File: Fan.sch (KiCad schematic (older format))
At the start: 0 parts

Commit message: Created CurrentDriver, Relay, and PowerProtection modules
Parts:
- added Q?: MOSFET_N, ~, symbol MOSFET_N
- added R? (x4): R, ~, symbol R
- added RV?: POT, ~, symbol POT
- added U?: LM324, symbol LM324
- added U?: MCP4922-E/P, DIP14, symbol MCP4922-E/P
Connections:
- net labels added: +12V, -12V, AGND, CS_N, Current Measure, MISO, MOSI, SCLK
- wire segments 0 -> 29

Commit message: Current driver refactoring, LED module, Arduino
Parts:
- removed R? (x2): R, ~, symbol R
- removed RV?: POT, ~, symbol POT
- added D?: DIODE, ~, symbol DIODE
- added Q? (x2): MOSFET_N, ~, symbol MOSFET_N
- added TH?: THERMISTOR, ~, symbol THERMISTOR
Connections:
- net labels added: +12C, CURR_MEAS, FAN_MODE, FAN_OUT+, FAN_OUT-, FAN_PWM, TACH_IN, TACH_MEAS
- net labels removed: Current Measure, Fan_In, Power+, Power-, Tach, Tach_out
- wire segments 29 -> 34
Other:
- moved on the sheet: R?, U?
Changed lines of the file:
@@
 Comment4 ""
 $EndDescr
-Text HLabel 10150 3200 0    60   Output ~ 0
-Power+
-Text HLabel 10150 3550 0    60   Input ~ 0
-Power-
-Text HLabel 10150 3950 0    60   Input ~ 0
-Tach
-Text HLabel 1400 4950 0    60   Output ~ 0
-Tach_out
-Text HLabel 1400 3650 0    60   Input ~ 0
-Fan_In
+Text HLabel 9950 1700 2    60   Output ~ 0
+FAN_OUT+
+Text HLabel 9950 2000 2    60   Output ~ 0
+FAN_OUT-
+Text HLabel 10400 6150 2    60   Input ~ 0
+TACH_IN
+Text HLabel 1400 6150 0    60   Output ~ 0
+TACH_MEAS
+Text HLabel 1300 3650 0    60   Input ~ 0
+FAN_PWM
 $Comp
 L LM324 U?
@@
 $EndComp
 $Comp
-L +12V #PWR?
-U 1 1 52F44494
-P 6600 1950
-F 0 "#PWR?" H 6600 1900 20  0001 C CNN
-F 1 "+12V" H 6600 2050 30  0000 C CNN
-F 2 "" H 6600 1950 60  0000 C CNN
-F 3 "" H 6600 1950 60  0000 C CNN
-	1    6600 1950
-	1    0    0    -1
-$EndComp
-$Comp
 L R R?
 U 1 1 52F444AC
@@
 L AGND #PWR?
 U 1 1 52F444C1
-P 6600 4750
-F 0 "#PWR?" H 6600 4750 40  0001 C CNN
-F 1 "AGND" H 6600 4680 50  0000 C CNN
-F 2 "" H 6600 4750 60  0000 C CNN
-F 3 "" H 6600 4750 60  0000 C CNN
-	1    6600 4750
+P 6600 4900
+F 0 "#PWR?" H 6600 4900 40  0001 C CNN
+F 1 "AGND" H 6600 4830 50  0000 C CNN
+F 2 "" H 6600 4900 60  0000 C CNN
+F 3 "" H 6600 4900 60  0000 C CNN
+	1    6600 4900
 	1    0    0    -1
 $EndComp
@@
 $EndComp
 $Comp
+L AGND #PWR?
+U 1 1 52F44588
+P 3700 3500
+F 0 "#PWR?" H 3700 3500 40  0001 C CNN
+F 1 "AGND" H 3700 3430 50  0000 C CNN
+F 2 "" H 3700 3500 60  0000 C CNN
+F 3 "" H 3700 3500 60  0000 C CNN
+	1    3700 3500
+	1    0    0    -1
+$EndComp
+$Comp
+L MCP4922-E/P U?
+U 1 1 52F445A1
+P 2100 2550
+F 0 "U?" H 2250 2950 40  0000 L BNN
+F 1 "MCP4922-E/P" H 2250 2900 40  0000 L BNN
+F 2 "DIP14" H 2100 2550 30  0000 C CIN
+F 3 "" H 2100 2550 60  0000 C CNN
+	1    2100 2550
+	1    0    0    -1
+$EndComp
+Text HLabel 1300 3850 0    60   Output ~ 0
+CURR_MEAS
+Text HLabel 1000 2350 0    60   Input ~ 0
+MOSI
+Text HLabel 1000 2650 0    60   Output ~ 0
+MISO
+Text HLabel 1000 2550 0    60   Input ~ 0
+CS_N
+Text HLabel 1000 2450 0    60   Input ~ 0
+SCLK
+Wire Wire Line
+	5450 2500 6300 2500
+Wire Wire Line
+	6600 2700 6600 4100
+Wire Wire Line
+	6600 4600 6600 4900
+Wire Wire Line
+	4100 3550 4100 2600
+Wire Wire Line
+	4100 2600 4450 2600
+Connection ~ 6600 3550
+Wire Wire Line
+	4850 1950 4850 2100
+Wire Wire Line
+	4850 3000 4850 2900
+Wire Wire Line
+	1300 3850 6600 3850
+Connection ~ 6600 3850
+Wire Wire Line
+	1000 2350 1550 2350
+Wire Wire Line
+	1000 2450 1550 2450
+Wire Wire Line
+	1000 2550 1550 2550
+$Comp
 L R R?
 U 1 1 52F44520
-P 3300 2050
-F 0 "R?" V 3380 2050 40  0000 C CNN
-F 1 "R" V 3307 2051 40  0000 C CNN
-F 2 "~" V 3230 2050 30  0000 C CNN
-F 3 "~" H 3300 2050 30  0000 C CNN
-	1    3300 2050
-	1    0    0    -1
-$EndComp
-$Comp
-L +12V #PWR?
-U 1 1 52F44526
-P 3300 1700
-F 0 "#PWR?" H 3300 1650 20  0001 C CNN
-F 1 "+12V" H 3300 1800 30  0000 C CNN
-F 2 "" H 3300 1700 60  0000 C CNN
-F 3 "" H 3300 1700 60  0000 C CNN
-	1    3300 1700
-	1    0    0    -1
-$EndComp
-$Comp
-L POT RV?
-U 1 1 52F4455B
-P 3300 2800
-F 0 "RV?" H 3300 2700 50  0000 C CNN
-F 1 "POT" H 3300 2800 50  0000 C CNN
-F 2 "~" H 3300 2800 60  0000 C CNN
-F 3 "~" H 3300 2800 60  0000 C CNN
-	1    3300 2800
+P 3250 2400
+F 0 "R?" V 3330 2400 40  0000 C CNN
+F 1 "R" V 3257 2401 40  0000 C CNN
+F 2 "~" V 3180 2400 30  0000 C CNN
+F 3 "~" H 3250 2400 30  0000 C CNN
+	1    3250 2400
 	0    -1   -1   0
 $EndComp
-$Comp
-L AGND #PWR?
-U 1 1 52F44588
-P 3300 3250
-F 0 "#PWR?" H 3300 3250 40  0001 C CNN
-F 1 "AGND" H 3300 3180 50  0000 C CNN
-F 2 "" H 3300 3250 60  0000 C CNN
-F 3 "" H 3300 3250 60  0000 C CNN
-	1    3300 3250
-	1    0    0    -1
-$EndComp
-$Comp
-L MCP4922-E/P U?
-U 1 1 52F445A1
-P 2200 2500
-F 0 "U?" H 2350 2900 40  0000 L BNN
-F 1 "MCP4922-E/P" H 2350 2850 40  0000 L BNN
-F 2 "DIP14" H 2200 2500 30  0000 C CIN
-F 3 "" H 2200 2500 60  0000 C CNN
-	1    2200 2500
-	1    0    0    -1
-$EndComp
-Text HLabel 1400 3850 0    60   Output ~ 0
-Current Measure
-$Comp
-L R R?
-U 1 1 52F445E4
-P 3800 3050
-F 0 "R?" V 3880 3050 40  0000 C CNN
-F 1 "R" V 3807 3051 40  0000 C CNN
-F 2 "~" V 3730 3050 30  0000 C CNN
-F 3 "~" H 3800 3050 30  0000 C CNN
-	1    3800 3050
-	1    0    0    -1
-$EndComp
-Text HLabel 1100 2300 0    60   Input ~ 0
-MOSI
-Text HLabel 1100 2600 0    60   Output ~ 0
-MISO
-Text HLabel 1100 2500 0    60   Input ~ 0
-CS_N
-Text HLabel 1100 2400 0    60   Input ~ 0
-SCLK
-Wire Wire Line
-	5450 2500 6300 2500
-Wire Wire Line
-	6600 2700 6600 3200
-Wire Wire Line
-	6600 3200 10150 3200
-Wire Wire Line
-	4100 3550 10150 3550
-Wire Wire Line
-	6600 3550 6600 4100
-Wire Wire Line
-	6600 4750 6600 4600
-Wire Wire Line
-	4100 3550 4100 2600
-Wire Wire Line
-	4100 2600 4450 2600
-Connection ~ 6600 3550
-Wire Wire Line
-	6600 2300 6600 1950
-Wire Wire Line
-	4850 1950 4850 2100
-Wire Wire Line
-	4850 3000 4850 2900
-Wire Wire Line
-	3300 2400 4450 2400
-Wire Wire Line
-	3300 1700 3300 1800
-Wire Wire Line
-	3300 3250 3300 3050
-Wire Wire Line
-	1400 4950 9350 4950
-Wire Wire Line
-	9350 4950 9350 3950
-Wire Wire Line
-	9350 3950 10150 3950
-Wire Wire Line
-	1400 3850 5600 3850
-Wire Wire Line
-	5450 3850 6600 3850
-Connection ~ 6600 3850
-Wire Wire Line
-	3300 2300 3300 2550
-Connection ~ 3300 2400
-Wire Wire Line
-	3800 2800 3800 2400
-Connection ~ 3800 2400
-Wire Wire Line
-	1400 3650 3800 3650
-Wire Wire Line
-	3800 3650 3800 3300
-Wire Wire Line
-	1100 2300 1650 2300
-Wire Wire Line
-	1100 2400 1650 2400
-Wire Wire Line
-	1100 2500 1650 2500
-Wire Wire Line
-	1650 2700 1600 2700
-Connection ~ 1600 3650
-$Comp
-L R R?
-U 1 1 52F446FA
-P 1600 3200
-F 0 "R?" V 1680 3200 40  0000 C CNN
-F 1 "R" V 1607 3201 40  0000 C CNN
-F 2 "~" V 1530 3200 30  0000 C CNN
-F 3 "~" H 1600 3200 30  0000 C CNN
-	1    1600 3200
-	1    0    0    -1
-$EndComp
-Wire Wire Line
-	1600 3450 1600 3650
-Wire Wire Line
-	1600 2700 1600 2950
+Wire Wire Line
+	3000 2400 2650 2400
+$Comp
+L MOSFET_N Q?
+U 1 1 52F7C941
+P 5800 4350
+F 0 "Q?" H 5810 4520 60  0000 R CNN
+F 1 "MOSFET_N" H 5810 4200 60  0000 R CNN
+F 2 "~" H 5800 4350 60  0000 C CNN
+F 3 "~" H 5800 4350 60  0000 C CNN
+	1    5800 4350
+	1    0    0    -1
+$EndComp
+$Comp
+L THERMISTOR TH?
+U 1 1 52F7C9A5
+P 6600 1250
+F 0 "TH?" V 6700 1300 50  0000 C CNN
+F 1 "THERMISTOR" V 6500 1250 50  0000 C CNN
+F 2 "~" H 6600 1250 60  0000 C CNN
+F 3 "~" H 6600 1250 60  0000 C CNN
+	1    6600 1250
+	1    0    0    -1
+$EndComp
+Wire Wire Line
+	6600 1500 6600 1700
+Wire Wire Line
+	6600 1700 9950 1700
+Wire Wire Line
+	4100 3550 6600 3550
+Wire Wire Line
+	9950 2000 6600 2000
+Wire Wire Line
+	6600 2000 6600 2300
+Wire Wire Line
+	6600 900  6600 1000
+$Comp
+L DIODE D?
+U 1 1 52F7CA49
+P 6400 1800
+F 0 "D?" H 6400 1900 40  0000 C CNN
+F 1 "DIODE" H 6400 1700 40  0000 C CNN
+F 2 "~" H 6400 1800 60  0000 C CNN
+F 3 "~" H 6400 1800 60  0000 C CNN
+	1    6400 1800
+	0    -1   -1   0
+$EndComp
+Wire Wire Line
+	6400 2000 6400 2100
+Wire Wire Line
+	6400 2100 6600 2100
+Connection ~ 6600 2100
+Wire Wire Line
+	6400 1600 6400 1550
+Wire Wire Line
+	6400 1550 6600 1550
+Connection ~ 6600 1550
+Wire Wire Line
+	5900 4150 5900 4000
+Wire Wire Line
+	5900 4000 6600 4000
+Connection ~ 6600 4000
+Wire Wire Line
+	5900 4550 5900 4700
+Wire Wire Line
+	5900 4700 6600 4700
+Connection ~ 6600 4700
+Wire Wire Line
+	10400 6150 1400 6150
+Wire Wire Line
+	1300 3650 2850 3650
+Wire Wire Line
+	3500 2400 4450 2400
+$Comp
+L MOSFET_N Q?
+U 1 1 52F7CBE7
+P 3600 3100
+F 0 "Q?" H 3610 3270 60  0000 R CNN
+F 1 "MOSFET_N" H 3610 2950 60  0000 R CNN
+F 2 "~" H 3600 3100 60  0000 C CNN
+F 3 "~" H 3600 3100 60  0000 C CNN
+	1    3600 3100
+	1    0    0    -1
+$EndComp
+Wire Wire Line
+	3400 3100 2850 3100
+Wire Wire Line
+	2850 3100 2850 3650
+Wire Wire Line
+	3700 3500 3700 3300
+Wire Wire Line
+	3700 2900 3700 2400
+Connection ~ 3700 2400
+Wire Wire Line
+	5600 4350 1300 4350
+Text HLabel 1300 4350 0    60   Input ~ 0
+FAN_MODE
+$Comp
+L +12C #PWR?
+U 1 1 52F7D01B
+P 6600 900
+F 0 "#PWR?" H 6600 870 30  0001 C CNN
+F 1 "+12C" H 6600 1010 40  0000 C CNN
+F 2 "" H 6600 900 60  0000 C CNN
+F 3 "" H 6600 900 60  0000 C CNN
+	1    6600 900
+	1    0    0    -1
+$EndComp
 $EndSCHEMATC

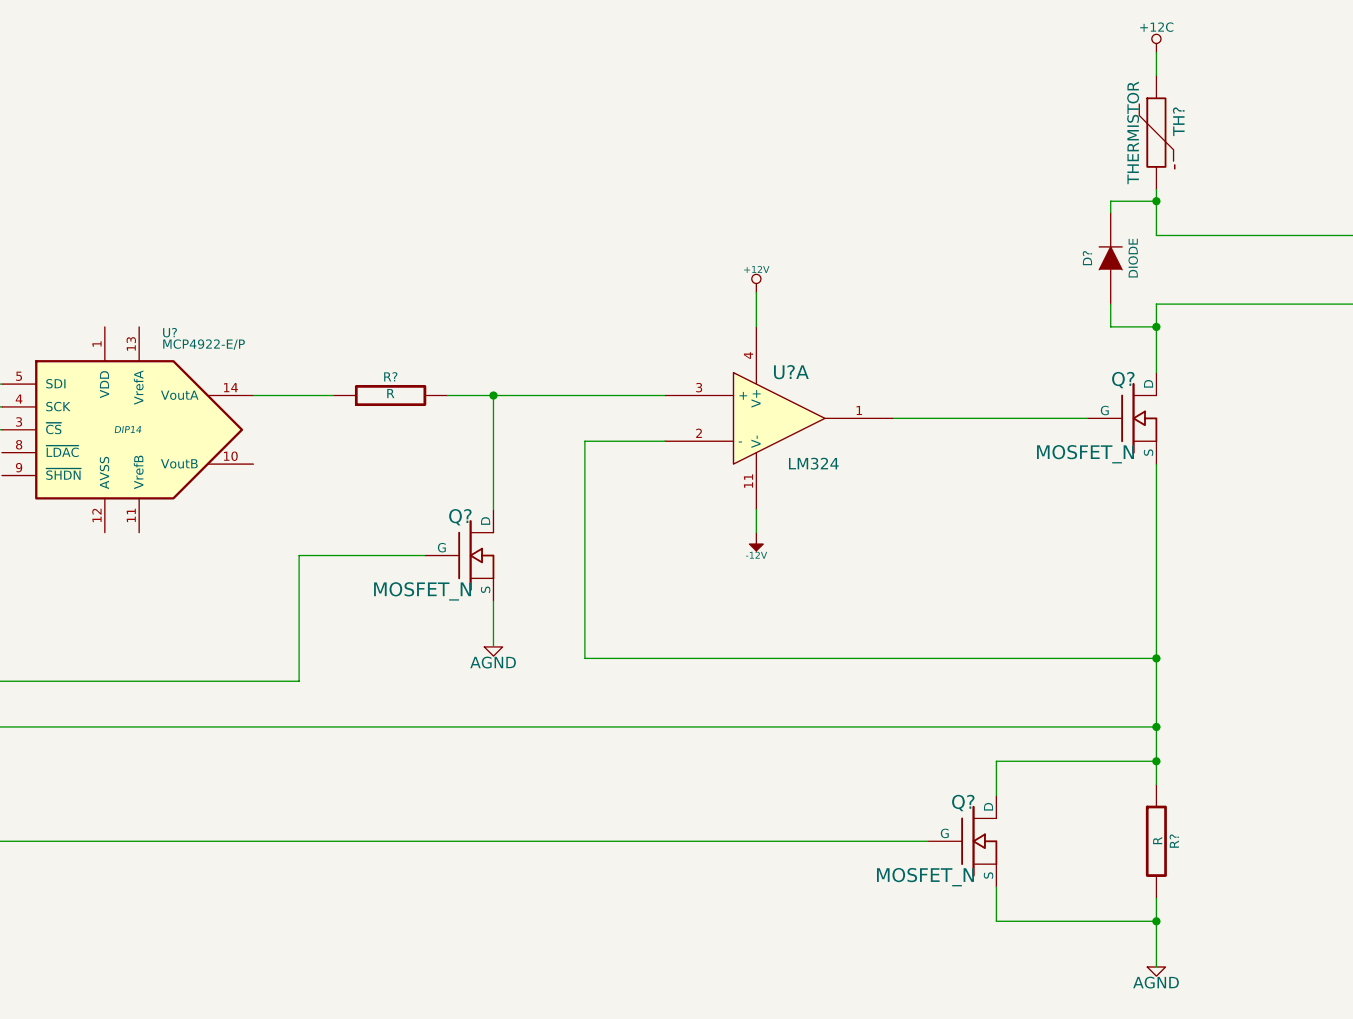
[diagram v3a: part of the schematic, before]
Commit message: Relay module association and placement
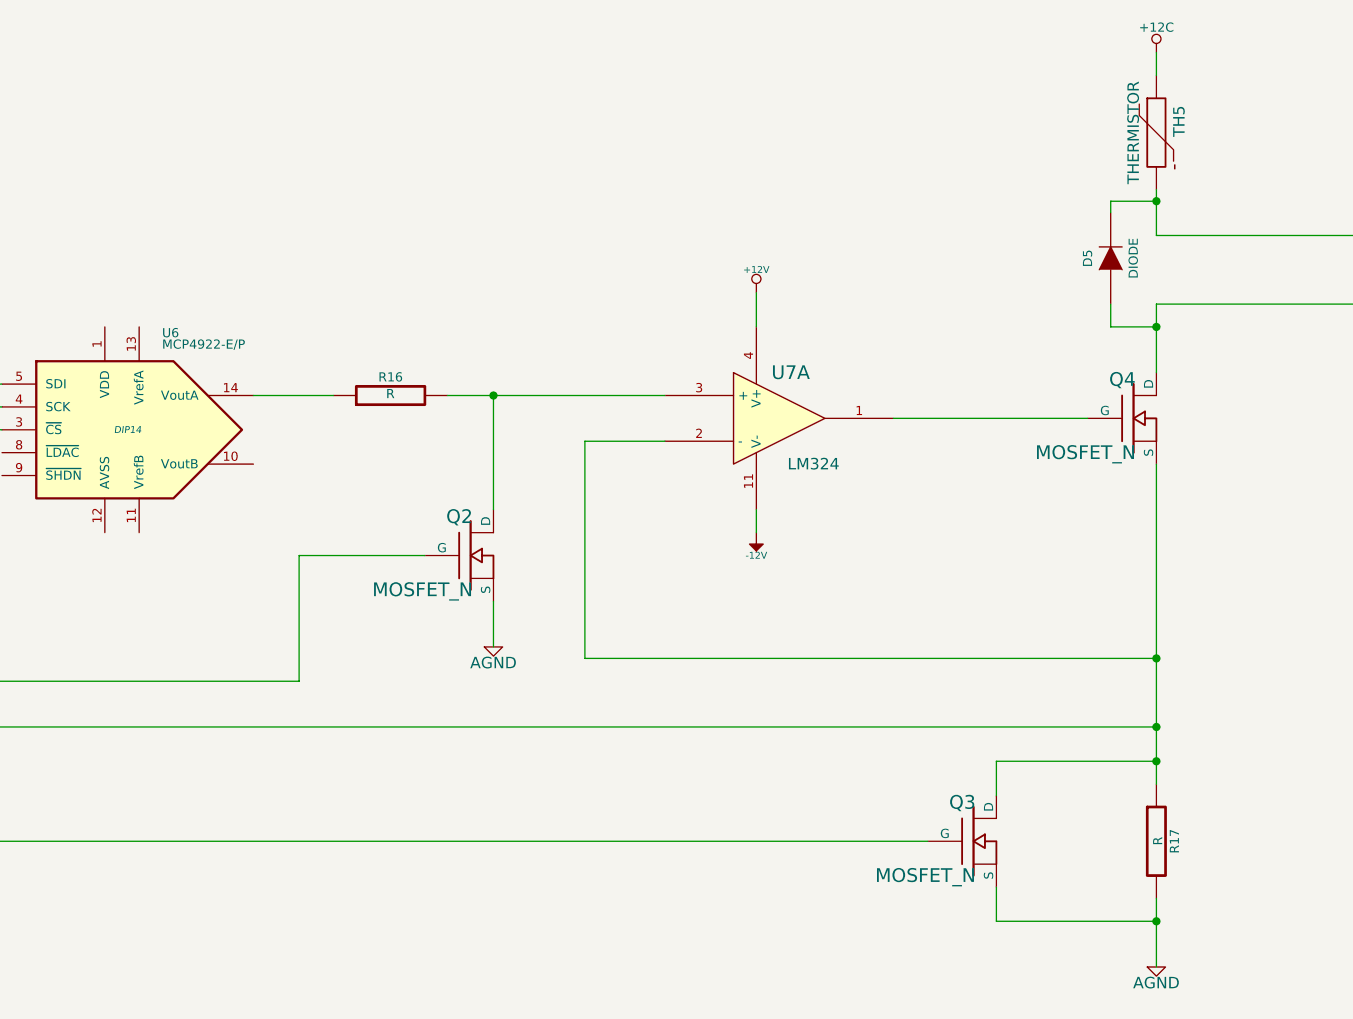
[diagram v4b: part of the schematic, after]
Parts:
- gave numbers to parts that had none: 9
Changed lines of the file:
@@
 Sheet 6 9
 Title ""
-Date "18 feb 2014"
+Date "20 feb 2014"
 Rev ""
 Comp ""
@@
 FAN_PWM
 $Comp
-L LM324 U?
+L LM324 U7
 U 1 1 52F44453
 P 4950 2500
-F 0 "U?" H 5000 2700 60  0000 C CNN
+F 0 "U7" H 5000 2700 60  0000 C CNN
 F 1 "LM324" H 5100 2300 50  0000 C CNN
 F 2 "" H 4950 2500 60  0000 C CNN
@@
 $EndComp
 $Comp
-L MOSFET_N Q?
+L MOSFET_N Q4
 U 1 1 52F44471
 P 6500 2500
-F 0 "Q?" H 6510 2670 60  0000 R CNN
+F 0 "Q4" H 6510 2670 60  0000 R CNN
 F 1 "MOSFET_N" H 6510 2350 60  0000 R CNN
 F 2 "~" H 6500 2500 60  0000 C CNN
@@
 $EndComp
 $Comp
-L R R?
+L R R17
 U 1 1 52F444AC
 P 6600 4350
-F 0 "R?" V 6680 4350 40  0000 C CNN
+F 0 "R17" V 6680 4350 40  0000 C CNN
 F 1 "R" V 6607 4351 40  0000 C CNN
 F 2 "~" V 6530 4350 30  0000 C CNN
@@
 $EndComp
 $Comp
-L AGND #PWR?
+L AGND #PWR029
 U 1 1 52F444C1
 P 6600 4900
-F 0 "#PWR?" H 6600 4900 40  0001 C CNN
+F 0 "#PWR029" H 6600 4900 40  0001 C CNN
 F 1 "AGND" H 6600 4830 50  0000 C CNN
 F 2 "" H 6600 4900 60  0000 C CNN
@@
 $EndComp
 $Comp
-L +12V #PWR?
+L +12V #PWR030
 U 1 1 52F444E6
 P 4850 1950
-F 0 "#PWR?" H 4850 1900 20  0001 C CNN
+F 0 "#PWR030" H 4850 1900 20  0001 C CNN
 F 1 "+12V" H 4850 2050 30  0000 C CNN
 F 2 "" H 4850 1950 60  0000 C CNN
@@
 $EndComp
 $Comp
-L -12V #PWR?
+L -12V #PWR031
 U 1 1 52F444F9
 P 4850 3000
-F 0 "#PWR?" H 4850 3130 20  0001 C CNN
+F 0 "#PWR031" H 4850 3130 20  0001 C CNN
 F 1 "-12V" H 4850 3100 30  0000 C CNN
 F 2 "" H 4850 3000 60  0000 C CNN
@@
 $EndComp
 $Comp
-L AGND #PWR?
+L AGND #PWR032
 U 1 1 52F44588
 P 3700 3500
-F 0 "#PWR?" H 3700 3500 40  0001 C CNN
+F 0 "#PWR032" H 3700 3500 40  0001 C CNN
 F 1 "AGND" H 3700 3430 50  0000 C CNN
 F 2 "" H 3700 3500 60  0000 C CNN
@@
 $EndComp
 $Comp
-L MCP4922-E/P U?
+L MCP4922-E/P U6
 U 1 1 52F445A1
 P 2100 2550
-F 0 "U?" H 2250 2950 40  0000 L BNN
+F 0 "U6" H 2250 2950 40  0000 L BNN
 F 1 "MCP4922-E/P" H 2250 2900 40  0000 L BNN
 F 2 "DIP14" H 2100 2550 30  0000 C CIN
@@
 	1000 2550 1550 2550
 $Comp
-L R R?
+L R R16
 U 1 1 52F44520
 P 3250 2400
-F 0 "R?" V 3330 2400 40  0000 C CNN
+F 0 "R16" V 3330 2400 40  0000 C CNN
 F 1 "R" V 3257 2401 40  0000 C CNN
 F 2 "~" V 3180 2400 30  0000 C CNN
@@
 	3000 2400 2650 2400
 $Comp
-L MOSFET_N Q?
+L MOSFET_N Q3
 U 1 1 52F7C941
 P 5800 4350
-F 0 "Q?" H 5810 4520 60  0000 R CNN
+F 0 "Q3" H 5810 4520 60  0000 R CNN
 F 1 "MOSFET_N" H 5810 4200 60  0000 R CNN
 F 2 "~" H 5800 4350 60  0000 C CNN
@@
 $EndComp
 $Comp
-L THERMISTOR TH?
+L THERMISTOR TH5
 U 1 1 52F7C9A5
 P 6600 1250
-F 0 "TH?" V 6700 1300 50  0000 C CNN
+F 0 "TH5" V 6700 1300 50  0000 C CNN
 F 1 "THERMISTOR" V 6500 1250 50  0000 C CNN
 F 2 "~" H 6600 1250 60  0000 C CNN
@@
 	6600 900  6600 1000
 $Comp
-L DIODE D?
+L DIODE D5
 U 1 1 52F7CA49
 P 6400 1800
-F 0 "D?" H 6400 1900 40  0000 C CNN
+F 0 "D5" H 6400 1900 40  0000 C CNN
 F 1 "DIODE" H 6400 1700 40  0000 C CNN
 F 2 "~" H 6400 1800 60  0000 C CNN
@@
 	3500 2400 4450 2400
 $Comp
-L MOSFET_N Q?
+L MOSFET_N Q2
 U 1 1 52F7CBE7
 P 3600 3100
-F 0 "Q?" H 3610 3270 60  0000 R CNN
+F 0 "Q2" H 3610 3270 60  0000 R CNN
 F 1 "MOSFET_N" H 3610 2950 60  0000 R CNN
 F 2 "~" H 3600 3100 60  0000 C CNN
@@
 FAN_MODE
 $Comp
-L +12C #PWR?
+L +12C #PWR033
 U 1 1 52F7D01B
 P 6600 900
-F 0 "#PWR?" H 6600 870 30  0001 C CNN
+F 0 "#PWR033" H 6600 870 30  0001 C CNN
 F 1 "+12C" H 6600 1010 40  0000 C CNN
 F 2 "" H 6600 900 60  0000 C CNN

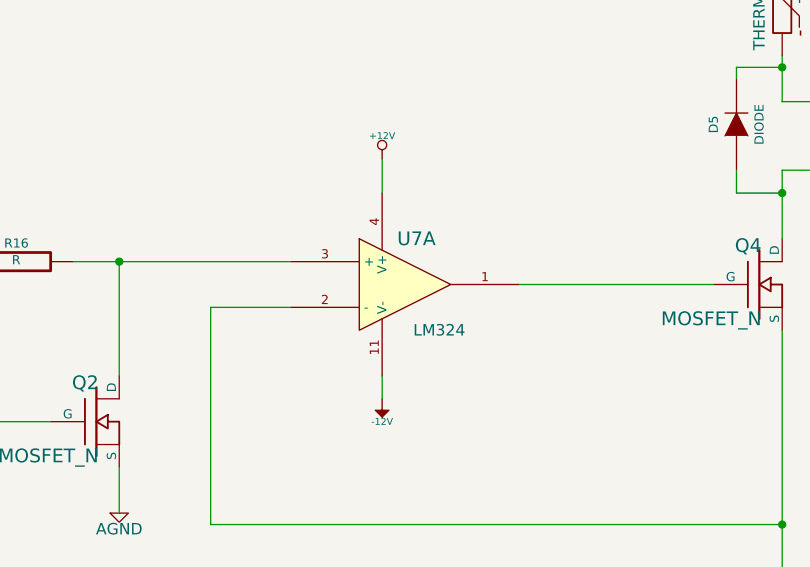
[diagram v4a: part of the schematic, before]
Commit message: Thermocouple association and placement
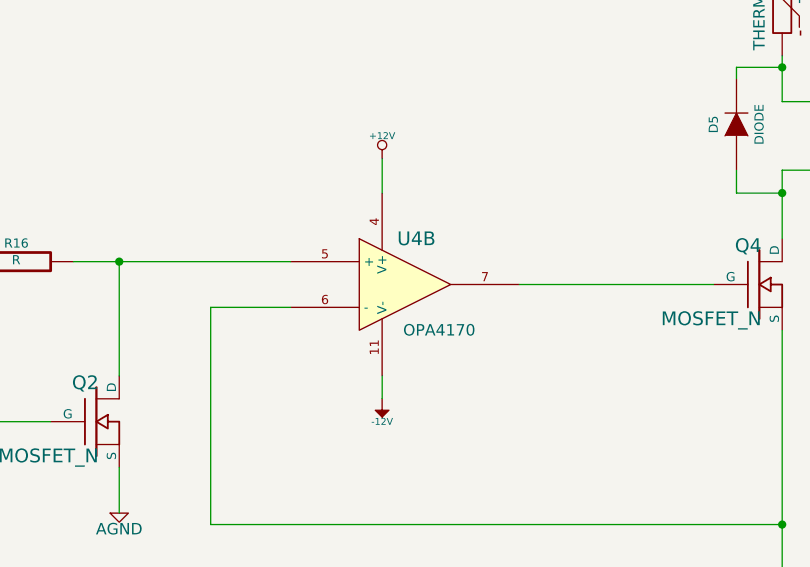
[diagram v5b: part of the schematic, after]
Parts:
- U4: renamed from U7; value LM324 -> OPA4170
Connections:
- net CURR_MEAS: now also U4.6 (-); no longer U4.2 (-)
- net at Q4.1 (G): now also U4.7; no longer U4.1
- net at Q2.2 (D), R16.2: now also U4.5 (+); no longer U4.3 (+)
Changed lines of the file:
@@
 $Descr A4 11693 8268
 encoding utf-8
-Sheet 6 9
+Sheet 5 9
 Title ""
-Date "20 feb 2014"
+Date "21 feb 2014"
 Rev ""
 Comp ""
@@
 FAN_PWM
 $Comp
-L LM324 U7
-U 1 1 52F44453
+L LM324 U4
+U 2 1 52F44453
 P 4950 2500
-F 0 "U7" H 5000 2700 60  0000 C CNN
-F 1 "LM324" H 5100 2300 50  0000 C CNN
+F 0 "U4" H 5000 2700 60  0000 C CNN
+F 1 "OPA4170" H 5100 2300 50  0000 C CNN
 F 2 "" H 4950 2500 60  0000 C CNN
 F 3 "" H 4950 2500 60  0000 C CNN
-	1    4950 2500
+	2    4950 2500
 	1    0    0    -1
 $EndComp
@@
 $EndComp
 $Comp
-L AGND #PWR029
+L AGND #PWR25
 U 1 1 52F444C1
 P 6600 4900
-F 0 "#PWR029" H 6600 4900 40  0001 C CNN
+F 0 "#PWR25" H 6600 4900 40  0001 C CNN
 F 1 "AGND" H 6600 4830 50  0000 C CNN
 F 2 "" H 6600 4900 60  0000 C CNN
@@
 $EndComp
 $Comp
-L +12V #PWR030
+L +12V #PWR22
 U 1 1 52F444E6
 P 4850 1950
-F 0 "#PWR030" H 4850 1900 20  0001 C CNN
+F 0 "#PWR22" H 4850 1900 20  0001 C CNN
 F 1 "+12V" H 4850 2050 30  0000 C CNN
 F 2 "" H 4850 1950 60  0000 C CNN
@@
 $EndComp
 $Comp
-L -12V #PWR031
+L -12V #PWR23
 U 1 1 52F444F9
 P 4850 3000
-F 0 "#PWR031" H 4850 3130 20  0001 C CNN
+F 0 "#PWR23" H 4850 3130 20  0001 C CNN
 F 1 "-12V" H 4850 3100 30  0000 C CNN
 F 2 "" H 4850 3000 60  0000 C CNN
@@
 $EndComp
 $Comp
-L AGND #PWR032
+L AGND #PWR21
 U 1 1 52F44588
 P 3700 3500
-F 0 "#PWR032" H 3700 3500 40  0001 C CNN
+F 0 "#PWR21" H 3700 3500 40  0001 C CNN
 F 1 "AGND" H 3700 3430 50  0000 C CNN
 F 2 "" H 3700 3500 60  0000 C CNN
@@
 FAN_MODE
 $Comp
-L +12C #PWR033
+L +12C #PWR24
 U 1 1 52F7D01B
 P 6600 900
-F 0 "#PWR033" H 6600 870 30  0001 C CNN
+F 0 "#PWR24" H 6600 870 30  0001 C CNN
 F 1 "+12C" H 6600 1010 40  0000 C CNN
 F 2 "" H 6600 900 60  0000 C CNN
